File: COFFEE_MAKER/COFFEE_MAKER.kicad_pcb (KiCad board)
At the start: 2 copper layers, 54 parts, among them J1 Conn_01x03_Pin, J2 Conn_01x06, J3 Conn_01x03_Pin, J4 Screw_Terminal_01x02, J5 USB_C_Receptacle_USB2.0_16P, J7 Conn_01x04, Q1 BC850, SW5 Reset, SW6 Boot, U1 OKI-78SR-3.3_1.5-W36H-C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

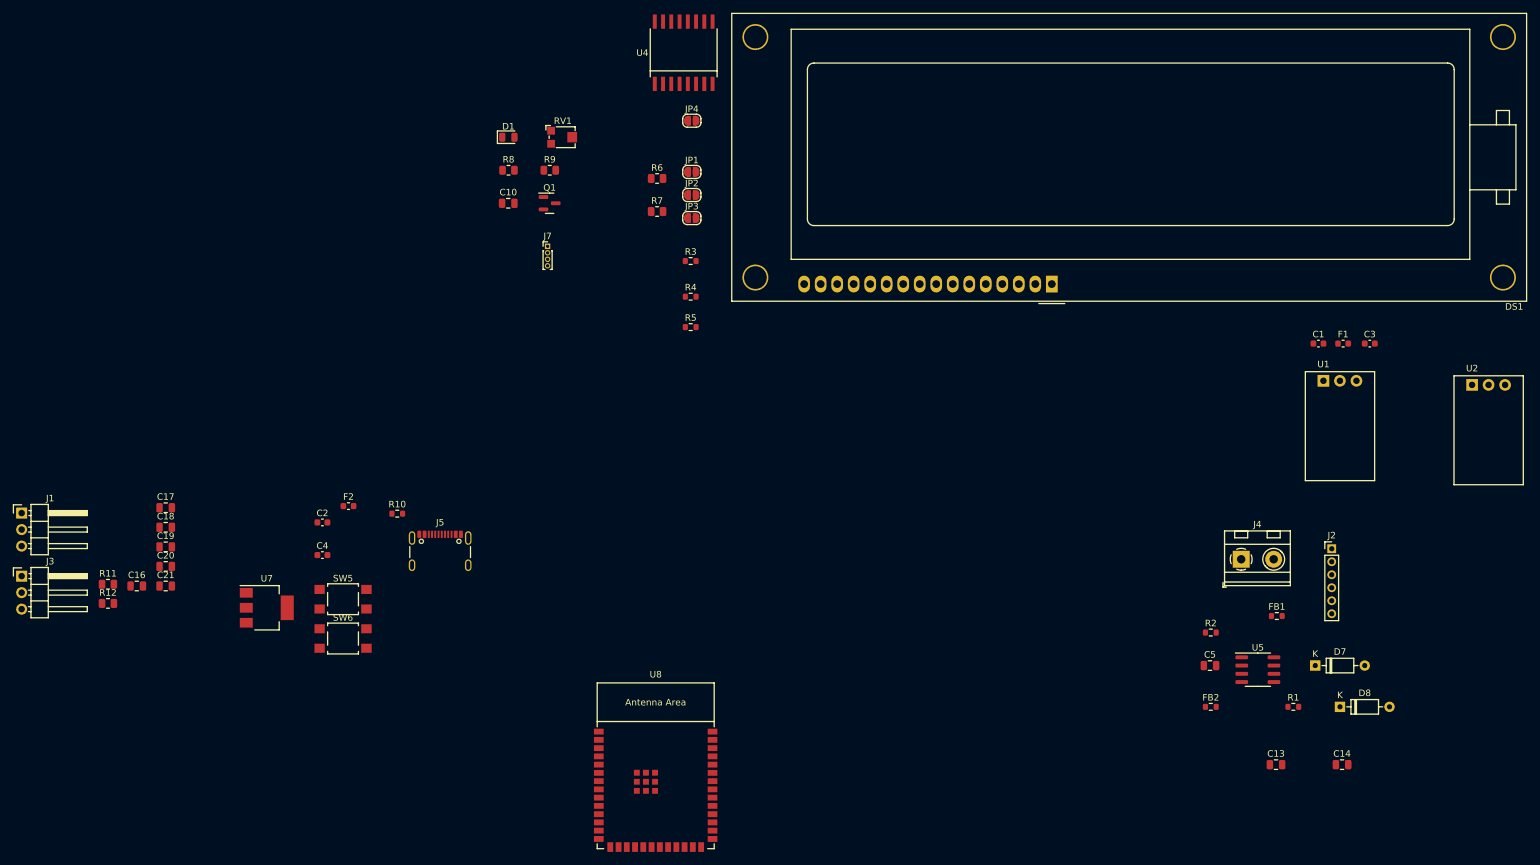
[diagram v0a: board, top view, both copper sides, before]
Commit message: board layout wip 27 errors
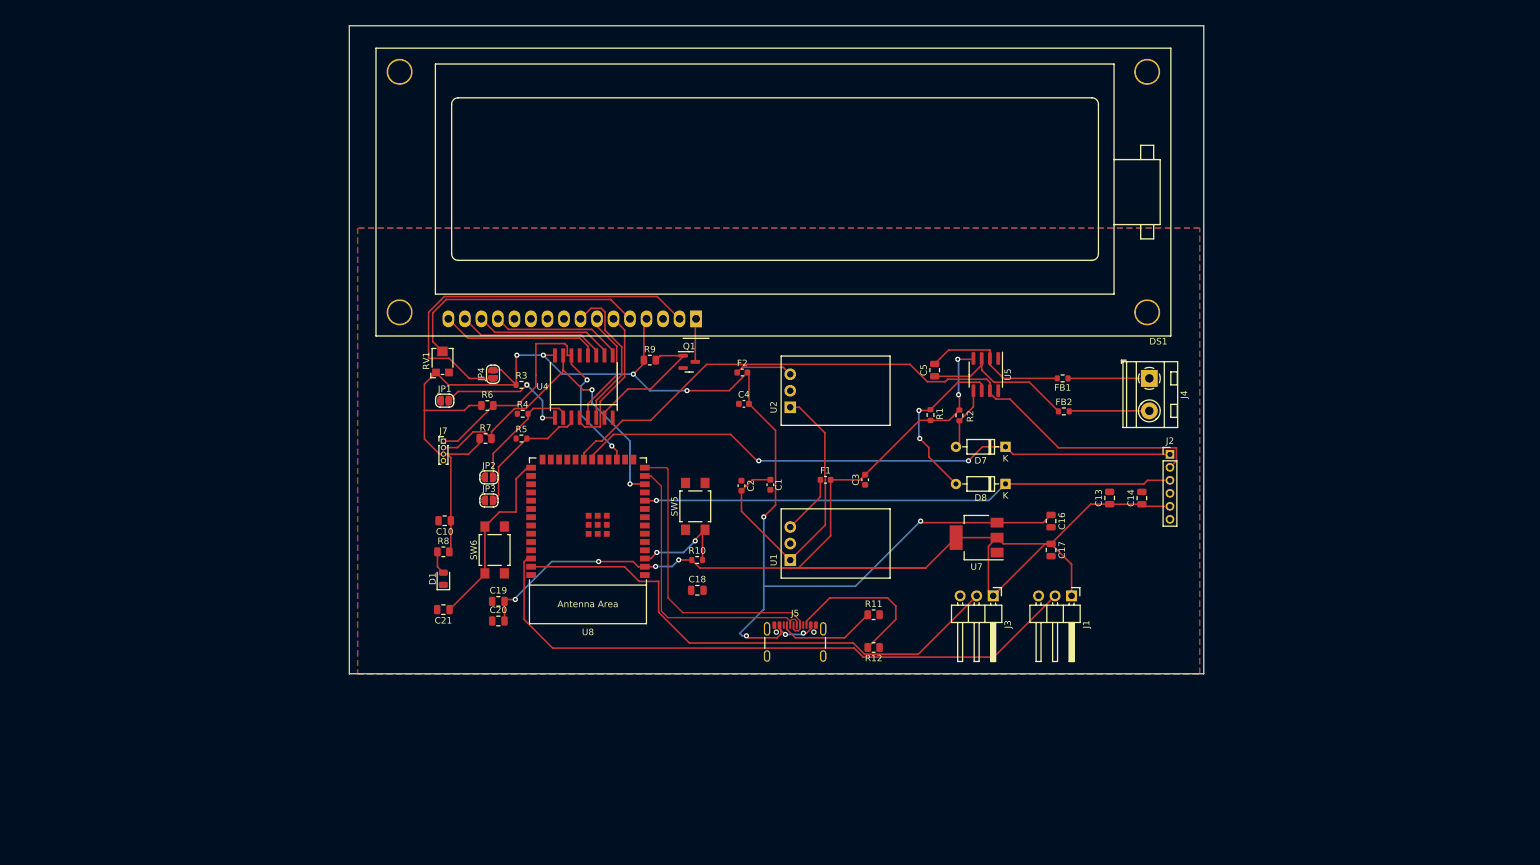
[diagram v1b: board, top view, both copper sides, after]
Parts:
- moved J1 162.0 mm to (208.9, 107.4), turned to -90 degrees
- moved J3 149.5 mm to (196.8, 107.4), turned to -90 degrees
- moved C16 141.0 mm to (205.7, 95.9), turned to -90 degrees
- moved C17 136.4 mm to (205.7, 100.3), turned to -90 degrees
- moved R12 118.0 mm to (178.4, 115.3), turned to 180 degrees
- moved R11 117.9 mm to (178.4, 110.3)
- moved U7 109.7 mm to (194.3, 98.4), turned to 180 degrees
- moved U2 105.0 mm to (165.6, 78.4), turned to 90 degrees
- moved C1 87.1 mm to (162.6, 90.3), turned to 90 degrees
- moved U1 86.5 mm to (165.6, 101.9), turned to 90 degrees
- moved C18 82.4 mm to (151.3, 106.5)
- moved F1 82.3 mm to (171.0, 89.5)
- moved C3 80.4 mm to (177.1, 89.5), turned to 90 degrees
- moved R1 71.6 mm to (187.2, 79.6), turned to -90 degrees
- moved C4 68.9 mm to (158.5, 77.9)
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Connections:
- C17 pad 1: +3.3V -> +3V3
- C19 pad 2: +3.3V -> +3V3
- C20 pad 2: +3.3V -> +3V3
- C3 pad 2: +3.3V -> +3V3
- F1 pad 2: +3.3V -> +3V3
- J1 pad 1: +3.3V -> +3V3
- J3 pad 1: +3.3V -> +3V3
- R10 pad 1: +3.3V -> +3V3
- U7 pad 2: +3.3V -> +3V3
- U8 pad 2: +3.3V -> +3V3
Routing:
- net +5V: track 0.00 -> 226.6 mm, vias 0 -> 9
- net +3V3: track 0.00 -> 218.0 mm, vias 0 -> 6
- net TC_so: track 0.00 -> 107.8 mm
- net RELAY_COIL: track 0.00 -> 98.2 mm
- net TC_sck: track 0.00 -> 93.9 mm, vias 0 -> 2
- net TC_cs: track 0.00 -> 82.1 mm, vias 0 -> 1
- net RELAY_FAN: track 0.00 -> 80.6 mm
- net Net-(DS1-LEDA): track 0.00 -> 59.3 mm
- net LCD_sda: track 0.00 -> 52.3 mm, vias 0 -> 2
- net LCD_scl: track 0.00 -> 51.1 mm, vias 0 -> 2
- net V_ALL+: track 0.00 -> 48.7 mm
- net /D+: track 0.00 -> 48.3 mm
- net /D-: track 0.00 -> 45.3 mm
- net Net-(DS1-Vo): track 0.00 -> 39.0 mm
- net Net-(U8-GPIO0): track 0.00 -> 28.9 mm
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- added copper zone on B.Cu, net GND
- added copper zone on F.Cu, net GND
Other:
- board outline added: 131.4 x 99.7 mm

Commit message: layout done, saved copy of slides
.Layout done, slides saved as ppt and pdf in folder, google slides here:
https://docs.google.com/presentation/d/1jqAALReZK5NcbOIQpBx0YGVnQ22f8MZOJf6NqvKvuig/edit#slide=id.g26e1c898e73_0_26
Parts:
- J7: footprint Connector_PinHeader_1.00mm:PinHeader_1x04_P1.00mm_Vertical -> Connector_PinHeader_2.00mm:PinHeader_1x04_P2.00mm_Vertical
- moved R12 5.83 mm to (183.7, 112.9)
- moved C20 3.18 mm to (119.2, 114.0)
- moved R11 2.76 mm to (179.3, 112.9)
- moved C18 2.16 mm to (152.4, 104.6)
- moved SW5 2.16 mm to (152.1, 91.7)
- moved R10 2.16 mm to (152.4, 100.0)
- moved C19 1.59 mm to (119.2, 108.7)
- moved SW6 1.44 mm to (118.9, 101.0)
- moved C1 1.17 mm to (162.6, 89.1)
- moved C2 1.17 mm to (158.1, 89.3)
- moved JP2 1.15 mm to (118.7, 88.1)
- moved JP3 0.74 mm to (118.7, 93.2)
- moved Q1 0.37 mm to (150.4, 71.4)
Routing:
- net +3V3: track 218.0 -> 194.5 mm
- net RELAY_FAN: track 80.6 -> 87.1 mm, vias 0 -> 2
- net V_ALL+: track 48.7 -> 54.4 mm
- net RELAY_COIL: track 98.2 -> 102.7 mm, vias 0 -> 2
- net +5V: track 226.6 -> 222.7 mm, vias 9 -> 8
- net Net-(J5-CC2): track 24.5 -> 22.6 mm
- net Net-(U8-EN): track 16.0 -> 17.9 mm
- net Net-(JP3-B): track 20.3 -> 21.1 mm
- net Net-(JP2-B): track 18.8 -> 18.1 mm
- net /D+: track 48.3 -> 47.7 mm
- net /D-: track 45.3 -> 44.7 mm
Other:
- board text added: "LCD I2C"
- board text added: "Microcontroller"
- board text added: "Thermocouple module"
- board text added: "VUSB to 3.3V"
- board text added: "Voltage drop down Regulators"

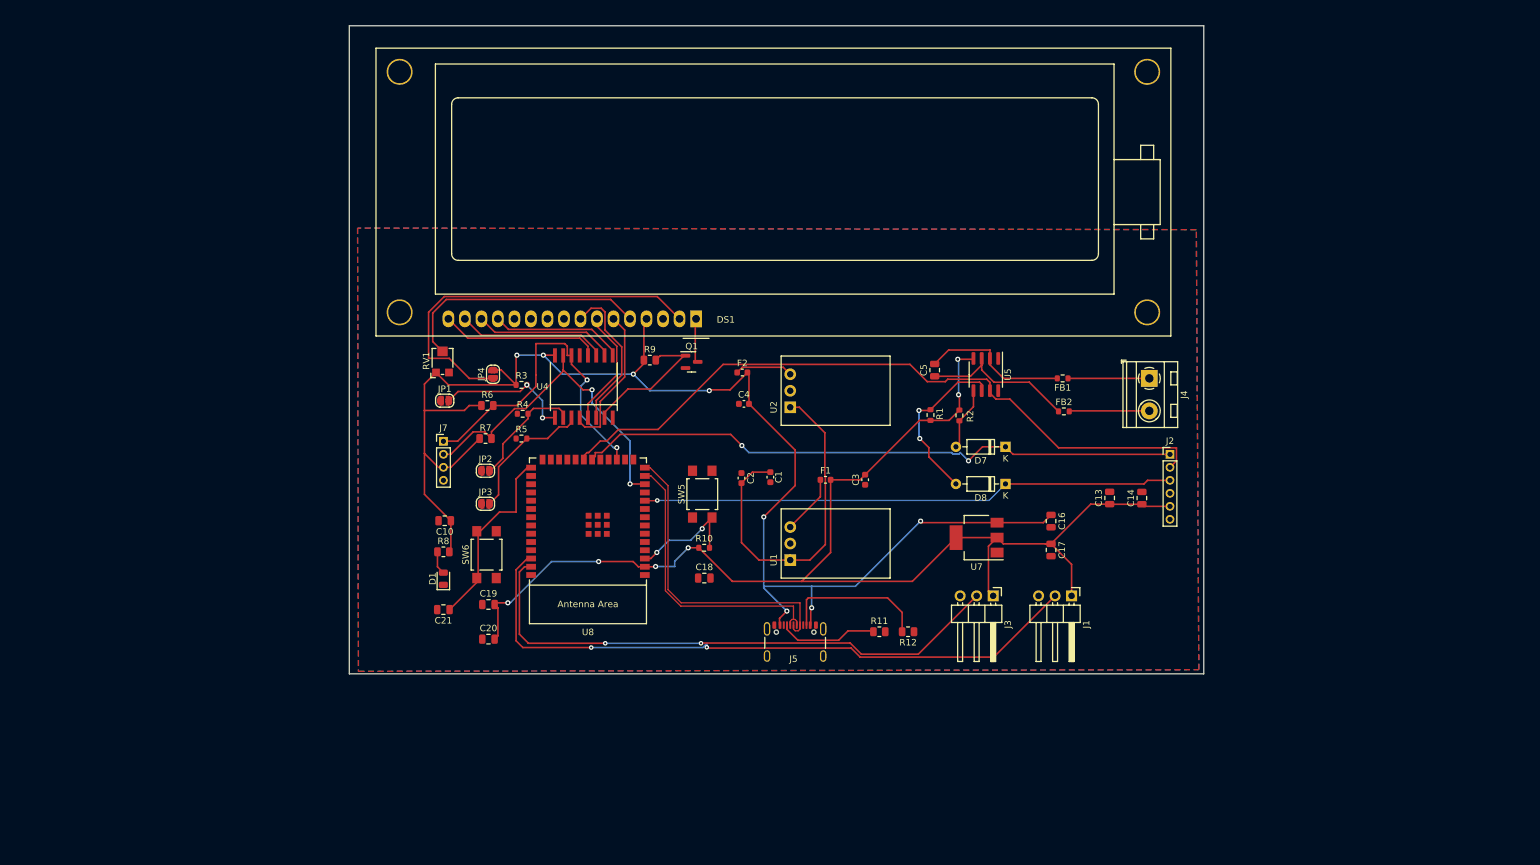
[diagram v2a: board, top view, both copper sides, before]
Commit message: layout mask to silkscreen fix
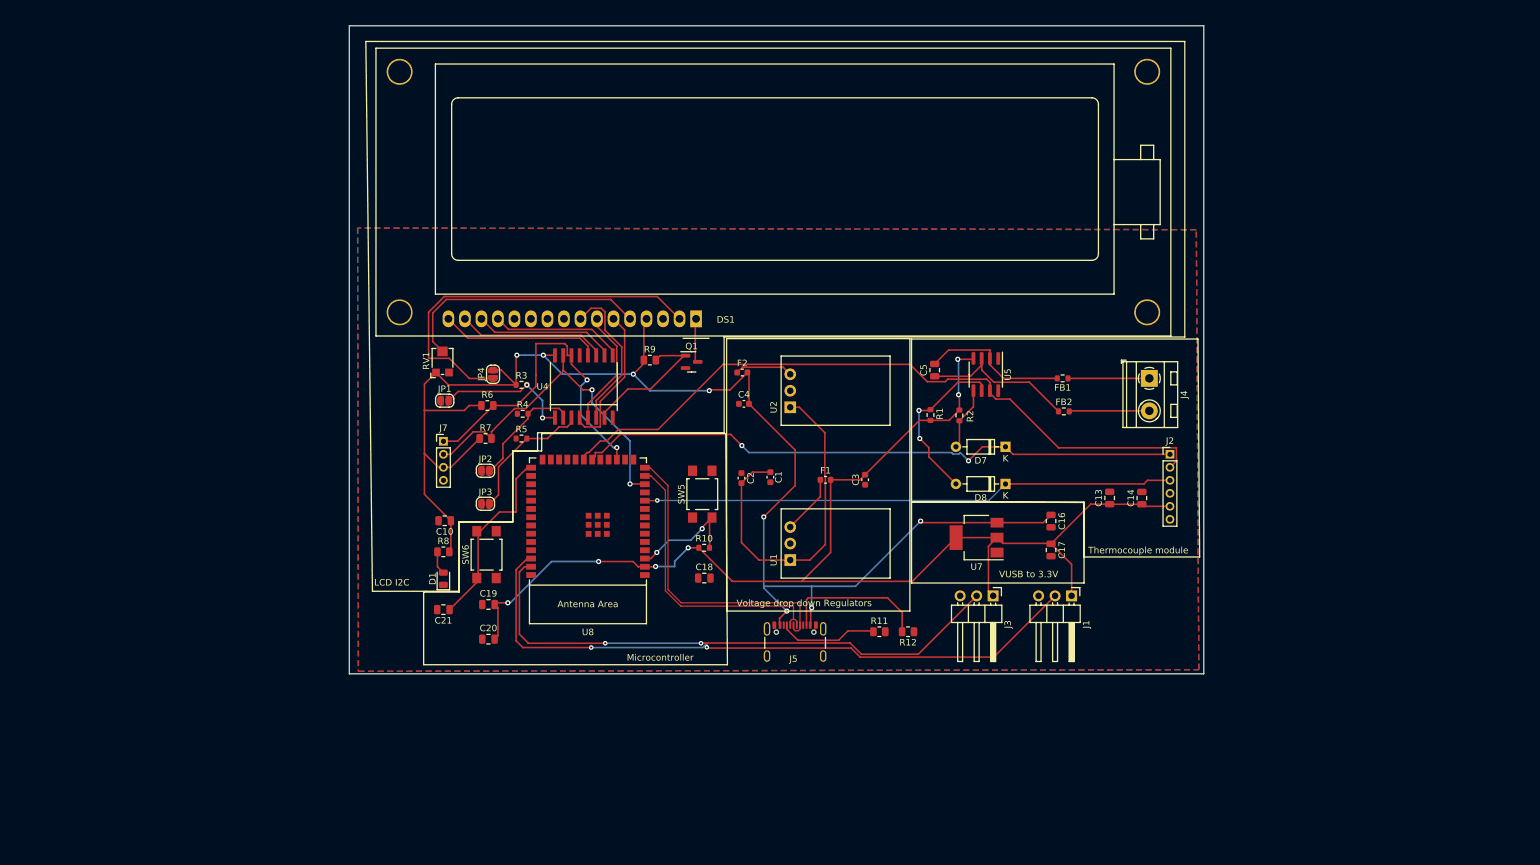
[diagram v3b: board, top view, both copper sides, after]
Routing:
- net +3V3: track 194.5 -> 193.6 mm
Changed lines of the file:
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@@
     )
   )
-  (gr_rect (start 184.277 92.71) (end 210.82 105.156)
-    (stroke (width 0.15) (type default)) (fill none) (layer "F.Mask"))
+  (gr_rect (start 184.277 92.964) (end 210.82 105.41)
+    (stroke (width 0.15) (type default)) (fill none) (layer "F.SilkS"))
   (gr_poly
     (pts
@@
       (xy 155.956 117.983)
     )
-    (stroke (width 0.15) (type solid)) (fill none) (layer "F.Mask"))
+    (stroke (width 0.15) (type solid)) (fill none) (layer "F.SilkS"))
   (gr_poly
     (pts
@@
       (xy 114.681 106.68)
     )
-    (stroke (width 0.15) (type solid)) (fill none) (layer "F.Mask"))
+    (stroke (width 0.15) (type solid)) (fill none) (layer "F.SilkS"))
   (gr_rect (start 155.829 67.818) (end 184.023 109.728)
-    (stroke (width 0.15) (type default)) (fill none) (layer "F.Mask"))
+    (stroke (width 0.15) (type default)) (fill none) (layer "F.SilkS"))
   (gr_poly
     (pts
-      (xy 228.6 101.219)
-      (xy 210.82 101.219)
-      (xy 210.82 92.837)
-      (xy 184.277 92.71)
-      (xy 184.277 67.691)
-      (xy 228.346 67.691)
+      (xy 228.6 101.404331)
+      (xy 210.82 101.404331)
+      (xy 210.82 93.022331)
+      (xy 184.277 92.895331)
+      (xy 184.277 67.876331)
+      (xy 228.346 67.876331)
     )
-    (stroke (width 0.15) (type solid)) (fill none) (layer "F.Mask"))
-  (gr_rect (start 210.693 92.6846) (end 184.277 92.71)
-    (stroke (width 0.15) (type default)) (fill none) (layer "F.Mask"))
+    (stroke (width 0.15) (type solid)) (fill none) (layer "F.SilkS"))
   (gr_rect (start 97.79 19.685) (end 229.235 119.38)
     (stroke (width 0.1) (type default)) (fill none) (layer "Edge.Cuts"))
-  (gr_text "Voltage drop down Regulators" (at 157.353 109.093) (layer "F.Mask")
+  (gr_text "Voltage drop down Regulators" (at 157.353 109.093) (layer "F.SilkS")
     (effects (font (size 1 1) (thickness 0.15)) (justify left bottom))
   )
-  (gr_text "Microcontroller" (at 140.462 117.475) (layer "F.Mask")
+  (gr_text "Microcontroller" (at 140.462 117.475) (layer "F.SilkS")
     (effects (font (size 1 1) (thickness 0.15)) (justify left bottom))
   )
-  (gr_text "LCD I2C" (at 101.6 105.918) (layer "F.Mask")
+  (gr_text "LCD I2C" (at 101.6 105.918) (layer "F.SilkS")
     (effects (font (size 1 1) (thickness 0.15)) (justify left bottom))
   )
-  (gr_text "Thermocouple module" (at 211.455 100.965) (layer "F.Mask")
+  (gr_text "Thermocouple module" (at 211.455 100.965) (layer "F.SilkS")
     (effects (font (size 1 1) (thickness 0.15)) (justify left bottom))
   )
-  (gr_text "VUSB to 3.3V" (at 197.739 104.648) (layer "F.Mask")
+  (gr_text "VUSB to 3.3V" (at 197.739 104.648) (layer "F.SilkS")
     (effects (font (size 1 1) (thickness 0.15)) (justify left bottom))
   )
@@
   (segment (start 211.841 93.279) (end 205.74 99.38) (width 0.25) (layer "F.Cu") (net 6))
   (segment (start 120.65 113.538) (end 120.65 109.22) (width 0.25) (layer "F.Cu") (net 6))
-  (segment (start 198.39 99.38) (end 197.435 98.425) (width 0.25) (layer "F.Cu") (net 6))
   (segment (start 214.77224 93.29424) (end 214.757 93.279) (width 0.25) (layer "F.Cu") (net 6))
   (segment (start 142.25062 102.90924) (end 141.44938 102.108) (width 0.25) (layer "F.Cu") (net 6))
@@
   (segment (start 176.3515 89.535) (end 177.1395 88.747) (width 0.25) (layer "F.Cu") (net 6))
   (segment (start 143.25062 102.90924) (end 144.86776 102.90924) (width 0.25) (layer "F.Cu") (net 6))
-  (segment (start 205.74 99.38) (end 204.84 99.38) (width 0.25) (layer "F.Cu") (net 6))
   (segment (start 171.831 100.711) (end 171.831 89.535) (width 0.25) (layer "F.Cu") (net 6))
   (segment (start 191.135 98.425) (end 197.435 98.425) (width 0.25) (layer "F.Cu") (net 6))
   (segment (start 196.11 106.66) (end 196.11 99.75) (width 0.25) (layer "F.Cu") (net 6))
+  (segment (start 205.674 99.314) (end 198.324 99.314) (width 0.25) (layer "F.Cu") (net 6))
   (segment (start 187.198 80.391) (end 190.056 80.391) (width 0.25) (layer "F.Cu") (net 6))
   (segment (start 120.396 108.458) (end 120.142 108.712) (width 0.25) (layer "F.Cu") (net 6))
@@
   (segment (start 224.03562 93.61424) (end 220.03 93.61424) (width 0.25) (layer "F.Cu") (net 6))
   (segment (start 171.831 89.535) (end 176.3515 89.535) (width 0.25) (layer "F.Cu") (net 6))
+  (segment (start 198.324 99.314) (end 197.435 98.425) (width 0.25) (layer "F.Cu") (net 6))
   (segment (start 191.389 70.993) (end 193.675 70.993) (width 0.25) (layer "F.Cu") (net 6))
   (segment (start 184.404 105.156) (end 191.135 98.425) (width 0.25) (layer "F.Cu") (net 6))
@@
   (segment (start 196.11 99.75) (end 197.435 98.425) (width 0.25) (layer "F.Cu") (net 6))
   (segment (start 156.713 105.156) (end 167.386 105.156) (width 0.25) (layer "F.Cu") (net 6))
+  (segment (start 205.74 99.38) (end 205.674 99.314) (width 0.25) (layer "F.Cu") (net 6))
   (segment (start 219.71 93.29424) (end 214.77224 93.29424) (width 0.25) (layer "F.Cu") (net 6))
   (segment (start 143.25062 102.90924) (end 142.25062 102.90924) (width 0.25) (layer "F.Cu") (net 6))
-  (segment (start 205.74 99.38) (end 198.39 99.38) (width 0.25) (layer "F.Cu") (net 6))
   (segment (start 208.9 102.54) (end 208.9 107.385) (width 0.25) (layer "F.Cu") (net 6))
   (segment (start 185.4955 80.391) (end 177.1395 88.747) (width 0.25) (layer "F.Cu") (net 6))

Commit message: schematic bom wip
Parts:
- C1, C2: footprint Capacitor_SMD:C_0603_1608Metric -> Capacitor_SMD:C_0805_2012Metric
- C13, C14: value 10 uF -> 10uF
- C18, C20, C21: value .1uF -> 0.1uF
- C5: value 0.01 uF -> 0.01uF
- R11, R12: value 5.1 k -> 5.1k
- moved C1 0.51 mm to (163.1, 89.2)

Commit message: layout v1 done, slides, BOM, manufacturing folder ready
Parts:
- added J6: Barrel_Jack, Connector_BarrelJack:BarrelJack_CUI_PJ-102AH_Horizontal, F.Cu at (214.9, 111.6)
- J2: footprint Connector_PinHeader_2.00mm:PinHeader_1x06_P2.00mm_Vertical -> Connector_PinHeader_2.54mm:PinHeader_1x06_P2.54mm_Vertical
- moved C1 1.91 mm to (165.0, 89.2)
- moved C2 1.91 mm to (160.0, 89.3)
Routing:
- net V_ALL+: track 54.4 -> 86.2 mm
- net TC_so: track 107.6 -> 112.7 mm
- net +3V3: track 193.6 -> 196.9 mm, vias 6 -> 12
- net +5V: track 222.7 -> 220.8 mm, vias 8 -> 10
- net Net-(D8-A): track 26.2 -> 27.8 mm
- net Net-(DS1-LEDA): track 59.3 -> 60.5 mm, vias 0 -> 2
- net Net-(J5-CC2): track 22.6 -> 23.5 mm, vias 0 -> 2
- net TC_sck: track 94.1 -> 94.6 mm
